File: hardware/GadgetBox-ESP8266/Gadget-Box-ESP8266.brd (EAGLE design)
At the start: 93.5 x 53.5 mm, 33 parts, among them U1 MCP73831T-2ACI/OT, U2 AP2112-3.3

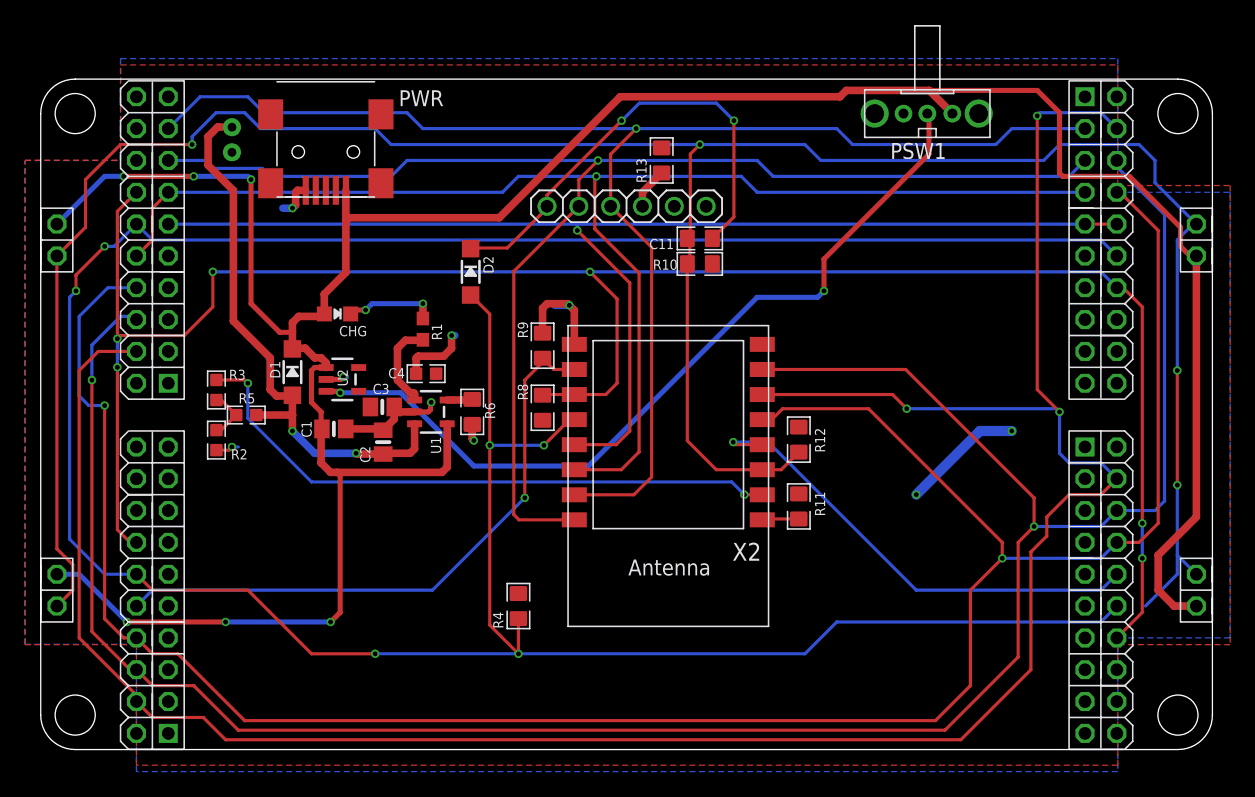
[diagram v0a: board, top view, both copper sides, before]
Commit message: Removed Alt eCog headers and re-routed outside traces.
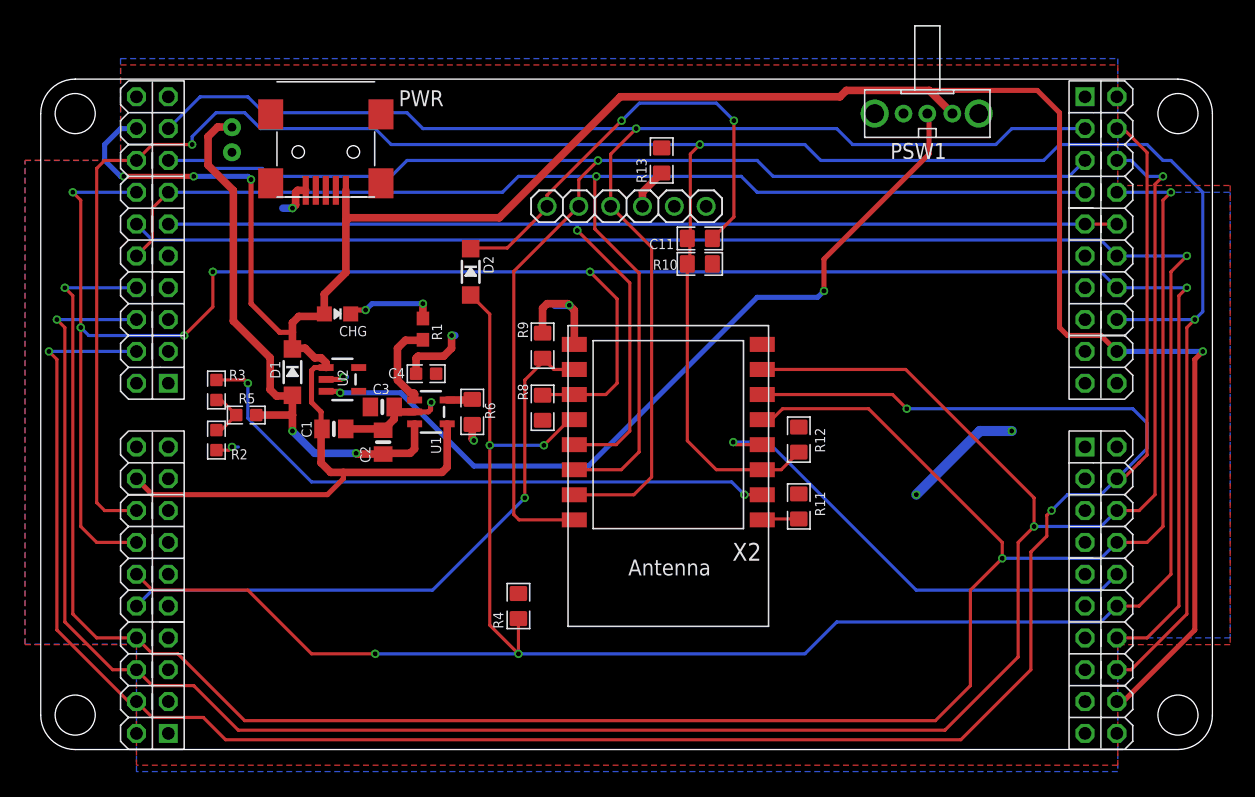
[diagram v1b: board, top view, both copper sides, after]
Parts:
- AH, AL, BH, BL: value ECOGECOG_SLOT_ALT1 -> ECOGECOG_SLOT; device eCogs:ECOG_ALT1 -> eCogs:ECOG
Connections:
- net 5V0: now also AH.5V@B7, AL.5V@B7, BH.5V@B7, BL.5V@B7; no longer AH.5V@2, AL.5V@2, BH.5V@2, BL.5V@2
- net RESET: now also AH.RESET@B6, AL.RESET@B6, BH.RESET@B6, BL.RESET@B6; no longer AH.RESET@2, AL.RESET@2, BH.RESET@2, BL.RESET@2
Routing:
- net I2C-SCL: track 159.7 -> 177.6 mm
- net 5V0: track 224.7 -> 216.0 mm, vias 6 -> 4
- net SPI-MISO: track 192.4 -> 200.4 mm
- net SPI-SCK: track 182.8 -> 189.9 mm, vias 2 -> 3
- net SPI-MOSI: track 186.2 -> 192.9 mm, vias 2 -> 3
- net RESET: track 202.2 -> 206.8 mm, vias 4 -> 3
- net I2C-SDA/BOOTLOAD: track 236.6 -> 239.2 mm, vias 6 -> 5
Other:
- board text added: "Gadget Box - ESP8266 Copyright 2016 Gadget Factory, LLC Version 1.2"
- board text removed: "Gadget Box - ESP8266 Copyright 2016 Gadget Factory, LLC Version 1.1"
